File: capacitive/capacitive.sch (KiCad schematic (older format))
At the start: 56 parts, among them J101 I2C, J102 UART, J103 SWD, J104 TX_PADS, J105 RX_PAD, J106 POWER, Q101 RU1C002ZPTCL, SW101 SW_Push, U101 STM32F070C6T6, U102 TLV9062IDR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

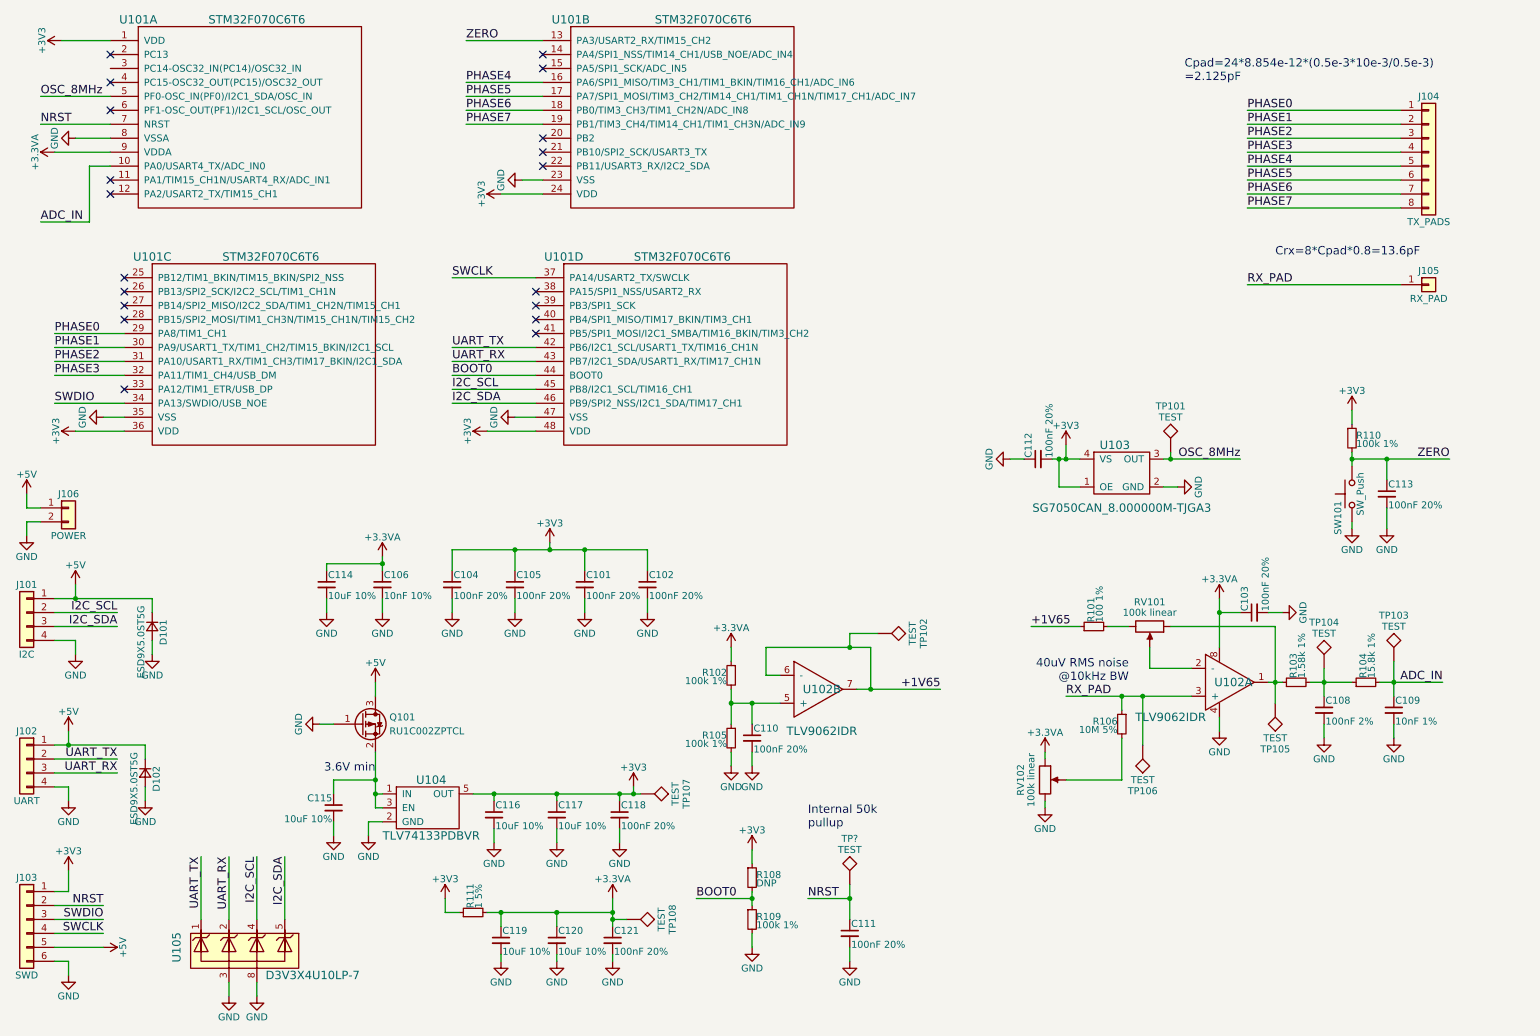
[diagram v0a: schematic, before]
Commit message: Start work on caliper scale generation
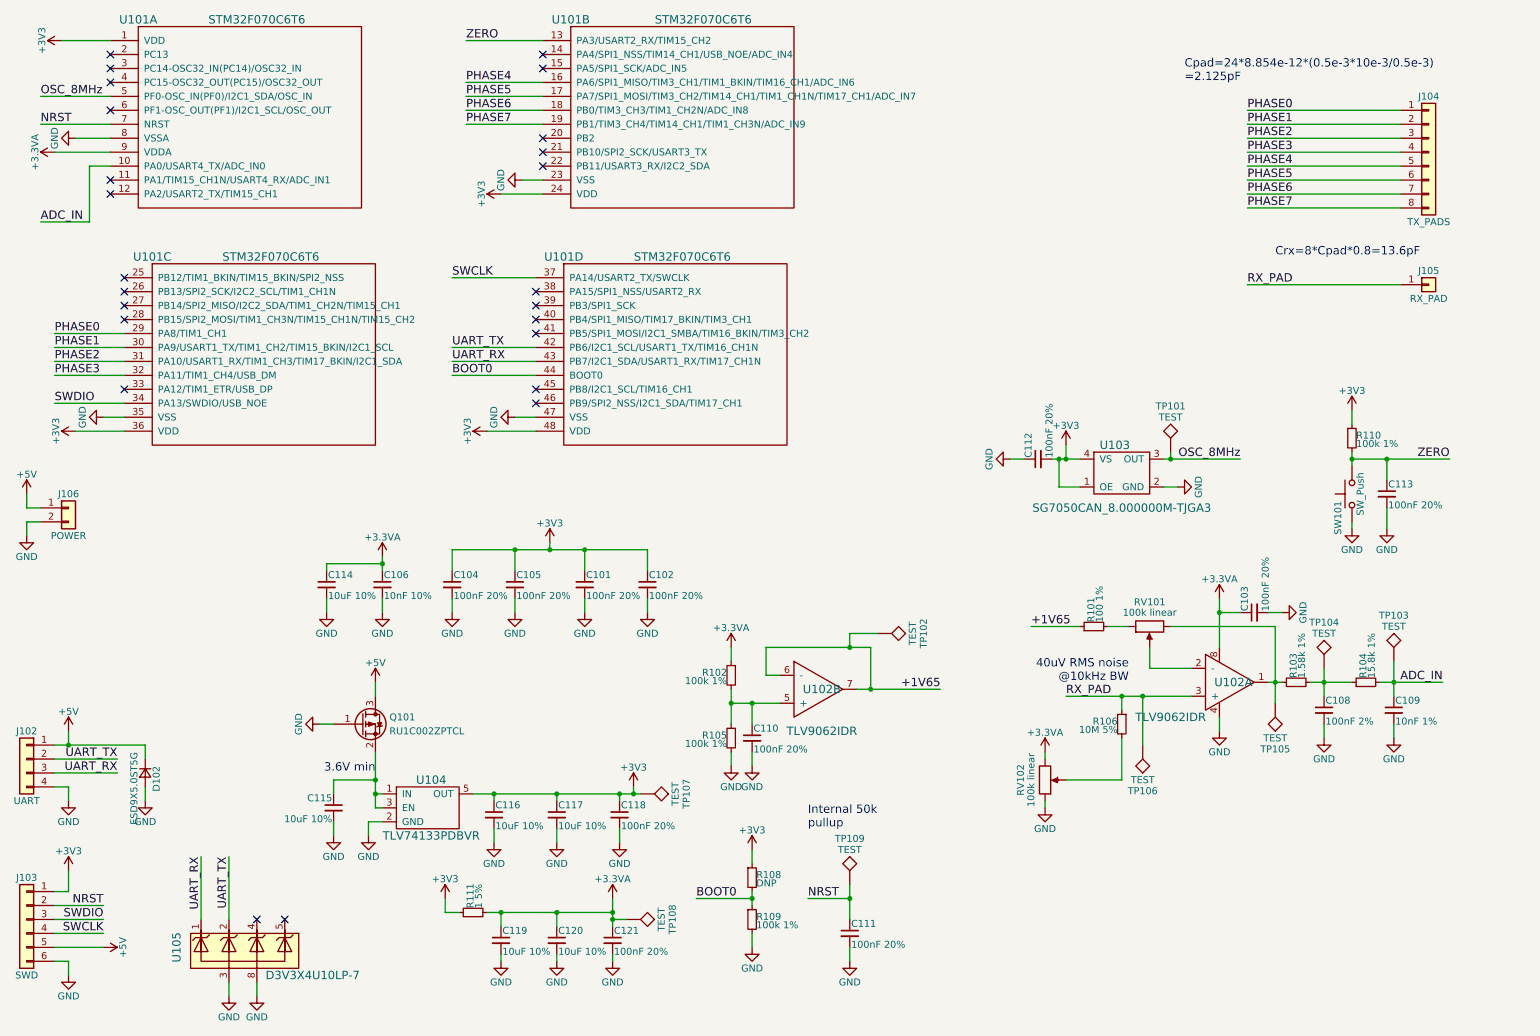
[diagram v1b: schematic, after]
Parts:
- removed D101: ESD9X5.0ST5G, capacitive:SOD-923, symbol D_Small
- removed J101: I2C, Socket_Strips:Socket_Strip_Straight_1x04_Pitch2.54mm, symbol Conn_01x04
- J104: footprint (none) -> capacitive:TX_PADS
- J105: footprint (none) -> capacitive:RX_PAD
- gave numbers to parts that had none: 1
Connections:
- net +3.3VA: now also RV102.3; no longer RV102.1
- net GND: now also RV102.1; no longer RV102.3
- net UART_RX: now also U105.1 (K1); no longer U105.2 (K2)
- net UART_TX: now also U105.2 (K2); no longer U105.1 (K1)
- net at R103.1, TP105.1, U102.1: now also RV101.3; no longer RV101.1
- net at R101.2: now also RV101.1; no longer RV101.3
- net I2C_SCL: no longer names the net of U101.45 (PB8/I2C1_SCL/TIM16_CH1)
- net I2C_SCL: no longer U105.4 (K3)
- net I2C_SDA: no longer names the net of U101.46 (PB9/SPI2_NSS/I2C1_SDA/TIM17_CH1)
- net I2C_SDA: no longer U105.5 (K4)
- no-connect marks 19 -> 24

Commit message: Add generation for holes
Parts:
- added J?: TEST_1P, symbol TEST_1P
- added R107, R112: 100k 1%, Resistors_SMD:R_1206_HandSoldering, symbol R_Small
- RV102: value 100k linear -> 5k linear; footprint capacitive:Vishay_T73YE -> capacitive:Bourns-PVG5H; Mouser 72-T70YE-100K -> 81-PVG5H502C03B00
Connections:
- net +3.3VA: now also R107.1; no longer RV102.3
- net GND: now also R112.2; no longer RV102.1
- new net: R107.2, RV102.1
- new net: R112.1, RV102.3
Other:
- note added: "approx 80mV swing"

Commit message: Generate first revision Gerber files
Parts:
- removed U105: D3V3X4U10LP-7, capacitive:Diode_U-DFN2510-10, symbol D3V3X4U10LP-7
- added C107: 100nF 20%, Capacitors_SMD:C_0805_HandSoldering, symbol C_Small
- added D101, D103: ESD9B3.3ST5G, capacitive:SOD-923, symbol D_TVS
- added J101: UL, capacitive:Slide_Drill_Left, symbol TEST_1P
- added J107: UR, capacitive:Slide_Drill_Right, symbol TEST_1P
- added J109: LR, capacitive:Slide_Drill_Right, symbol TEST_1P
- J108: renamed from J?; value TEST_1P -> LL; footprint (none) -> capacitive:Slide_Drill_Left; Mouser (none) -> NoPart
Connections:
- net GND: now also J108.1, C107.2, D101.2 (A2), D103.2 (A2), J101.1, J107.1, J109.1
- net PHASE0: now also U101.16 (PA6/SPI1_MISO/TIM3_CH1/TIM1_BKIN/TIM16_CH1/ADC_IN6); no longer U101.29 (PA8/TIM1_CH1)
- net PHASE1: now also U101.29 (PA8/TIM1_CH1); no longer U101.30 (PA9/USART1_TX/TIM1_CH2/TIM15_BKIN/I2C1_SCL)
- net PHASE2: now also U101.17 (PA7/SPI1_MOSI/TIM3_CH2/TIM14_CH1/TIM1_CH1N/TIM17_CH1/ADC_IN7); no longer U101.31 (PA10/USART1_RX/TIM1_CH3/TIM17_BKIN/I2C1_SDA)
- net PHASE3: now also U101.30 (PA9/USART1_TX/TIM1_CH2/TIM15_BKIN/I2C1_SCL); no longer U101.32 (PA11/TIM1_CH4/USB_DM)
- net PHASE4: now also U101.18 (PB0/TIM3_CH3/TIM1_CH2N/ADC_IN8); no longer U101.16 (PA6/SPI1_MISO/TIM3_CH1/TIM1_BKIN/TIM16_CH1/ADC_IN6)
- net PHASE5: now also U101.31 (PA10/USART1_RX/TIM1_CH3/TIM17_BKIN/I2C1_SDA); no longer U101.17 (PA7/SPI1_MOSI/TIM3_CH2/TIM14_CH1/TIM1_CH1N/TIM17_CH1/ADC_IN7)
- net PHASE6: now also U101.19 (PB1/TIM3_CH4/TIM14_CH1/TIM1_CH3N/ADC_IN9); no longer U101.18 (PB0/TIM3_CH3/TIM1_CH2N/ADC_IN8)
- net PHASE7: now also U101.32 (PA11/TIM1_CH4/USB_DM); no longer U101.19 (PB1/TIM3_CH4/TIM14_CH1/TIM1_CH3N/ADC_IN9)
- net UART_RX: now also D101.1 (A1)
- net UART_TX: now also D103.1 (A1)
- net at R103.1, TP105.1, U102.1: now also RV101.1; no longer RV101.3
- net at R101.2: now also RV101.3; no longer RV101.1
- net at R106.2, RV102.2: now also C107.1
- no-connect marks 24 -> 22
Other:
- moved on the sheet: J108

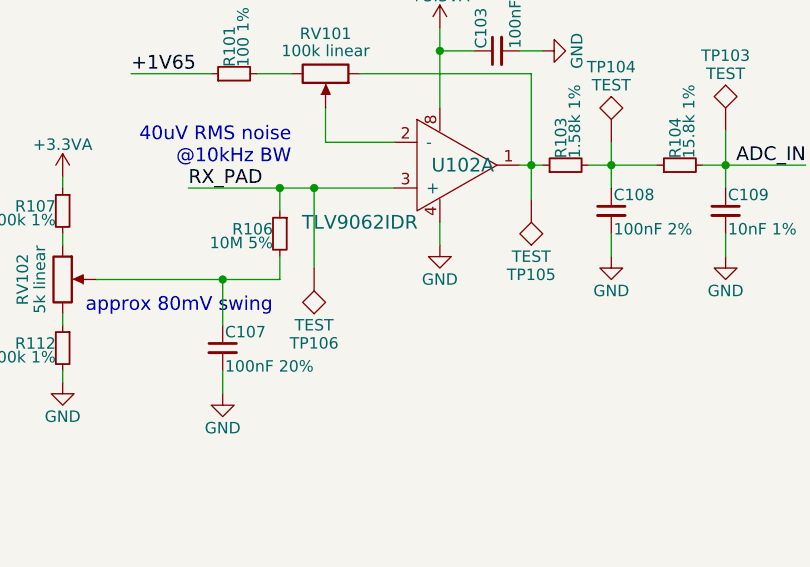
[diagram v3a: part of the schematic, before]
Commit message: Add input capacitor to help set the input roll-off frequency; it seems to reduce ripple a fair amount
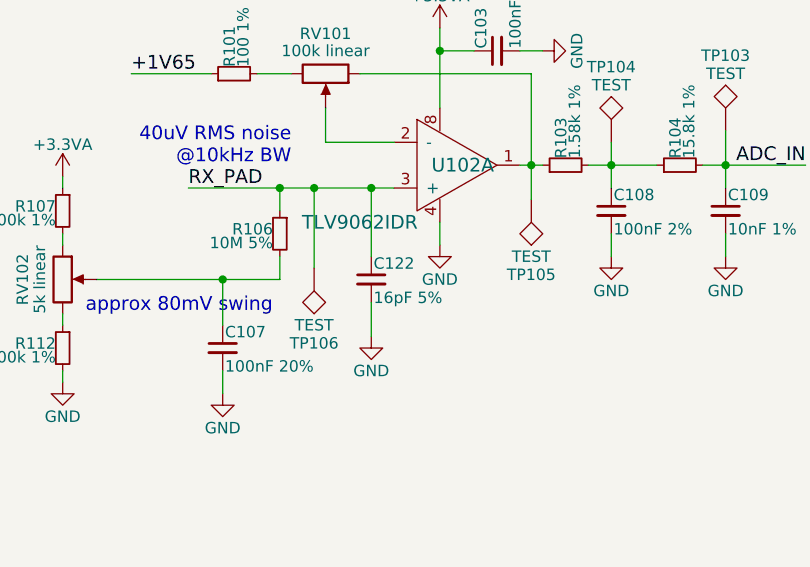
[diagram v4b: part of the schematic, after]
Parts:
- added C122: 16pF 5%, Capacitors_SMD:C_0603_HandSoldering, symbol C_Small
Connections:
- net GND: now also C122.2
- net RX_PAD: now also C122.1
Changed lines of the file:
@@
 $EndComp
 $Comp
-L +3V3 #PWR153
+L +3V3 #PWR154
 U 1 1 5B0020BC
 P 950 6700
-F 0 "#PWR153" H 950 6550 50  0001 C CNN
+F 0 "#PWR154" H 950 6550 50  0001 C CNN
 F 1 "+3V3" H 950 6840 50  0000 C CNN
 F 2 "" H 950 6700 50  0001 C CNN
@@
 $EndComp
 $Comp
-L GND #PWR162
+L GND #PWR163
 U 1 1 5B0020BD
 P 950 7450
-F 0 "#PWR162" H 950 7200 50  0001 C CNN
+F 0 "#PWR163" H 950 7200 50  0001 C CNN
 F 1 "GND" H 950 7300 50  0000 C CNN
 F 2 "" H 950 7450 50  0001 C CNN
@@
 $EndComp
 $Comp
-L GND #PWR143
+L GND #PWR144
 U 1 1 5B0020BE
 P 950 6200
-F 0 "#PWR143" H 950 5950 50  0001 C CNN
+F 0 "#PWR144" H 950 5950 50  0001 C CNN
 F 1 "GND" H 950 6050 50  0000 C CNN
 F 2 "" H 950 6200 50  0001 C CNN
@@
 SWDIO
 $Comp
-L +5V #PWR156
+L +5V #PWR157
 U 1 1 5B0020C0
 P 1200 7250
-F 0 "#PWR156" H 1200 7100 50  0001 C CNN
+F 0 "#PWR157" H 1200 7100 50  0001 C CNN
 F 1 "+5V" H 1200 7390 50  0000 C CNN
 F 2 "" H 1200 7250 50  0001 C CNN
@@
 $EndComp
 $Comp
-L GND #PWR157
+L GND #PWR158
 U 1 1 5B0020A3
 P 5850 7250
-F 0 "#PWR157" H 5850 7000 50  0001 C CNN
+F 0 "#PWR158" H 5850 7000 50  0001 C CNN
 F 1 "GND" H 5850 7100 50  0000 C CNN
 F 2 "" H 5850 7250 50  0001 C CNN
@@
 $EndComp
 $Comp
-L +3V3 #PWR152
+L +3V3 #PWR153
 U 1 1 5B0020A6
 P 5850 6550
-F 0 "#PWR152" H 5850 6400 50  0001 C CNN
+F 0 "#PWR153" H 5850 6400 50  0001 C CNN
 F 1 "+3V3" H 5850 6690 50  0000 C CNN
 F 2 "" H 5850 6550 50  0001 C CNN
@@
 $EndComp
 $Comp
-L GND #PWR161
+L GND #PWR162
 U 1 1 5B002089
 P 6550 7350
-F 0 "#PWR161" H 6550 7100 50  0001 C CNN
+F 0 "#PWR162" H 6550 7100 50  0001 C CNN
 F 1 "GND" H 6550 7200 50  0000 C CNN
 F 2 "" H 6550 7350 50  0001 C CNN
@@
 $EndComp
 $Comp
-L GND #PWR150
+L GND #PWR151
 U 1 1 5AFFF58F
 P 4450 6500
-F 0 "#PWR150" H 4450 6250 50  0001 C CNN
+F 0 "#PWR151" H 4450 6250 50  0001 C CNN
 F 1 "GND" H 4450 6350 50  0000 C CNN
 F 2 "" H 4450 6500 50  0001 C CNN
@@
 $EndComp
 $Comp
-L GND #PWR151
+L GND #PWR152
 U 1 1 5AFFF6A9
 P 4900 6500
-F 0 "#PWR151" H 4900 6250 50  0001 C CNN
+F 0 "#PWR152" H 4900 6250 50  0001 C CNN
 F 1 "GND" H 4900 6350 50  0000 C CNN
 F 2 "" H 4900 6500 50  0001 C CNN
@@
 $EndComp
 $Comp
-L GND #PWR149
+L GND #PWR150
 U 1 1 5AFFFA9C
 P 4000 6500
-F 0 "#PWR149" H 4000 6250 50  0001 C CNN
+F 0 "#PWR150" H 4000 6250 50  0001 C CNN
 F 1 "GND" H 4000 6350 50  0000 C CNN
 F 2 "" H 4000 6500 50  0001 C CNN
@@
 $EndComp
 $Comp
-L GND #PWR159
+L GND #PWR160
 U 1 1 5B000180
 P 4450 7350
-F 0 "#PWR159" H 4450 7100 50  0001 C CNN
+F 0 "#PWR160" H 4450 7100 50  0001 C CNN
 F 1 "GND" H 4450 7200 50  0000 C CNN
 F 2 "" H 4450 7350 50  0001 C CNN
@@
 $EndComp
 $Comp
-L GND #PWR160
+L GND #PWR161
 U 1 1 5B00029F
 P 4850 7350
-F 0 "#PWR160" H 4850 7100 50  0001 C CNN
+F 0 "#PWR161" H 4850 7100 50  0001 C CNN
 F 1 "GND" H 4850 7200 50  0000 C CNN
 F 2 "" H 4850 7350 50  0001 C CNN
@@
 $EndComp
 $Comp
-L +3.3VA #PWR155
+L +3.3VA #PWR156
 U 1 1 5B00067D
 P 4850 6900
-F 0 "#PWR155" H 4850 6750 50  0001 C CNN
+F 0 "#PWR156" H 4850 6750 50  0001 C CNN
 F 1 "+3.3VA" H 4850 7040 50  0000 C CNN
 F 2 "" H 4850 6900 50  0001 C CNN
@@
 PHASE2
 $Comp
-L GND #PWR148
+L GND #PWR149
 U 1 1 5B00F2B8
 P 3100 6450
-F 0 "#PWR148" H 3100 6200 50  0001 C CNN
+F 0 "#PWR149" H 3100 6200 50  0001 C CNN
 F 1 "GND" H 3100 6300 50  0000 C CNN
 F 2 "" H 3100 6450 50  0001 C CNN
@@
 $EndComp
 $Comp
-L GND #PWR158
+L GND #PWR159
 U 1 1 5B0030AB
 P 4050 7350
-F 0 "#PWR158" H 4050 7100 50  0001 C CNN
+F 0 "#PWR159" H 4050 7100 50  0001 C CNN
 F 1 "GND" H 4050 7200 50  0000 C CNN
 F 2 "" H 4050 7350 50  0001 C CNN
@@
 $EndComp
 $Comp
-L GND #PWR147
+L GND #PWR148
 U 1 1 5B003262
 P 2850 6450
-F 0 "#PWR147" H 2850 6200 50  0001 C CNN
+F 0 "#PWR148" H 2850 6200 50  0001 C CNN
 F 1 "GND" H 2850 6300 50  0000 C CNN
 F 2 "" H 2850 6450 50  0001 C CNN
@@
 $EndComp
 $Comp
-L GND #PWR145
+L GND #PWR146
 U 1 1 5B0035B2
 P 7550 6300
-F 0 "#PWR145" H 7550 6050 50  0001 C CNN
+F 0 "#PWR146" H 7550 6050 50  0001 C CNN
 F 1 "GND" H 7550 6150 50  0000 C CNN
 F 2 "" H 7550 6300 50  0001 C CNN
@@
 Connection ~ 4050 7000
 $Comp
-L +3V3 #PWR154
+L +3V3 #PWR155
 U 1 1 5B005AA3
 P 3650 6900
-F 0 "#PWR154" H 3650 6750 50  0001 C CNN
+F 0 "#PWR155" H 3650 6750 50  0001 C CNN
 F 1 "+3V3" H 3650 7040 50  0000 C CNN
 F 2 "" H 3650 6900 50  0001 C CNN
@@
 Connection ~ 3200 4500
 $Comp
-L GND #PWR164
+L GND #PWR165
 U 1 1 5B009F64
 P 2200 7450
-F 0 "#PWR164" H 2200 7200 50  0001 C CNN
+F 0 "#PWR165" H 2200 7200 50  0001 C CNN
 F 1 "GND" H 2200 7300 50  0000 C CNN
 F 2 "" H 2200 7450 50  0001 C CNN
@@
 $EndComp
 $Comp
-L GND #PWR163
+L GND #PWR164
 U 1 1 5B00A44D
 P 1900 7450
-F 0 "#PWR163" H 1900 7200 50  0001 C CNN
+F 0 "#PWR164" H 1900 7200 50  0001 C CNN
 F 1 "GND" H 1900 7300 50  0000 C CNN
 F 2 "" H 1900 7450 50  0001 C CNN
@@
 $EndComp
 $Comp
-L GND #PWR144
+L GND #PWR145
 U 1 1 5B00AC1D
 P 1500 6200
-F 0 "#PWR144" H 1500 5950 50  0001 C CNN
+F 0 "#PWR145" H 1500 5950 50  0001 C CNN
 F 1 "GND" H 1500 6050 50  0000 C CNN
 F 2 "" H 1500 6200 50  0001 C CNN
@@
 $EndComp
 $Comp
-L GND #PWR146
+L GND #PWR147
 U 1 1 5B02C9E9
 P 8250 6350
-F 0 "#PWR146" H 8250 6100 50  0001 C CNN
+F 0 "#PWR147" H 8250 6100 50  0001 C CNN
 F 1 "GND" H 8250 6200 50  0000 C CNN
 F 2 "" H 8250 6350 50  0001 C CNN
@@
 	8250 6050 8250 5850
 Connection ~ 8250 5850
+$Comp
+L C_Small C122
+U 1 1 5B05E967
+P 8900 5850
+F 0 "C122" H 8910 5920 50  0000 L CNN
+F 1 "16pF 5%" H 8910 5770 50  0000 L CNN
+F 2 "Capacitors_SMD:C_0603_HandSoldering" H 8900 5850 50  0001 C CNN
+F 3 "" H 8900 5850 50  0001 C CNN
+F 4 "963-TMK042CG160JC-W" H 8900 5850 60  0001 C CNN "Mouser"
+	1    8900 5850
+	1    0    0    -1
+$EndComp
+Wire Wire Line
+	8900 5750 8900 5450
+Connection ~ 8900 5450
+$Comp
+L GND #PWR143
+U 1 1 5B05EC7C
+P 8900 6100
+F 0 "#PWR143" H 8900 5850 50  0001 C CNN
+F 1 "GND" H 8900 5950 50  0000 C CNN
+F 2 "" H 8900 6100 50  0001 C CNN
+F 3 "" H 8900 6100 50  0001 C CNN
+	1    8900 6100
+	1    0    0    -1
+$EndComp
+Wire Wire Line
+	8900 5950 8900 6100
 $EndSCHEMATC

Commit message: Generate BOM
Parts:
- C106: Mouser VJ0603Y103KXAAC -> 80-C0603C103M5RAUTO
- R104: Mouser ERJ-8ENF1582V -> 667-ERJ-8ENF1582V
